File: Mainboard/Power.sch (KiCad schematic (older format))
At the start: 21 parts, among them Q1 P-Channel, U11 LP5907MFX-3.3, U4 TPS62175DQC, U5 TPS2113A

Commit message: Modify library references
As described in the README of the newly added libraries submodule.
Schematic and PCB are synced.

Hardware folder is renamed to mainboard
Any other PCBs can be put in their own subfolder in the gitrepo

Commit also swaps source/drain of Q1 because it appeared wrong for some
reason after updating all symbol/footprints.
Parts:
- L1: footprint ZOUDIOfootprints:SRN4012TA -> ZOUDIO-footprints:SRN4012TA
- Q1: footprint ZOUDIOfootprints:SOIC8_mosfet -> ZOUDIO-footprints:SOIC8_mosfet; symbol ZOUDIOsymbols:P-channel_SOIC -> Device:Q_PMOS_GSD
- U5: symbol ZOUDIOsymbols:TPS2113A -> ZOUDIO-symbols:TPS2113A
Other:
- moved on the sheet: R1
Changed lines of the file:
@@
 $EndDescr
-$Comp
-L ZOUDIOsymbols:P-channel_SOIC Q?
-U 1 1 60B84DA8
-P 2650 5000
-AR Path="/60B84DA8" Ref="Q?"  Part="1"
-AR Path="/60AAD6DF/60B84DA8" Ref="Q?"  Part="1"
-AR Path="/60B7AC16/60B84DA8" Ref="Q1"  Part="1"
-F 0 "Q1" H 2650 5247 60  0000 C CNN
-F 1 "P-Channel" H 2650 5141 60  0000 C CNN
-F 2 "ZOUDIOfootprints:SOIC8_mosfet" H 2650 5000 60  0001 C CNN
-F 3 "" H 2650 5000 60  0001 C CNN
-	1    2650 5000
-	-1   0    0    -1
-$EndComp
 $Comp
 L Device:R_Small R?
 U 1 1 60B84DAE
-P 2650 5450
+P 2650 5500
 AR Path="/60B84DAE" Ref="R?"  Part="1"
 AR Path="/60AAD6DF/60B84DAE" Ref="R?"  Part="1"
 AR Path="/60B7AC16/60B84DAE" Ref="R1"  Part="1"
-F 0 "R1" H 2709 5496 50  0000 L CNN
-F 1 "1M" H 2709 5405 50  0000 L CNN
-F 2 "Resistor_SMD:R_0603_1608Metric" H 2650 5450 50  0001 C CNN
-F 3 "~" H 2650 5450 50  0001 C CNN
-	1    2650 5450
+F 0 "R1" H 2709 5546 50  0000 L CNN
+F 1 "1M" H 2709 5455 50  0000 L CNN
+F 2 "Resistor_SMD:R_0603_1608Metric" H 2650 5500 50  0001 C CNN
+F 3 "~" H 2650 5500 50  0001 C CNN
+	1    2650 5500
 	1    0    0    -1
 $EndComp
@@
 L power:GND #PWR?
 U 1 1 60B84DB4
-P 2650 5600
+P 2650 5650
 AR Path="/60B84DB4" Ref="#PWR?"  Part="1"
 AR Path="/60AAD6DF/60B84DB4" Ref="#PWR?"  Part="1"
 AR Path="/60B7AC16/60B84DB4" Ref="#PWR0124"  Part="1"
-F 0 "#PWR0124" H 2650 5350 50  0001 C CNN
-F 1 "GND" H 2655 5427 50  0001 C CNN
-F 2 "" H 2650 5600 50  0001 C CNN
-F 3 "" H 2650 5600 50  0001 C CNN
-	1    2650 5600
-	1    0    0    -1
-$EndComp
-Wire Wire Line
-	2650 5600 2650 5550
+F 0 "#PWR0124" H 2650 5400 50  0001 C CNN
+F 1 "GND" H 2655 5477 50  0001 C CNN
+F 2 "" H 2650 5650 50  0001 C CNN
+F 3 "" H 2650 5650 50  0001 C CNN
+	1    2650 5650
+	1    0    0    -1
+$EndComp
+Wire Wire Line
+	2650 5650 2650 5600
 $Comp
 L power:GND #PWR?
 U 1 1 60B84DBC
-P 2350 5600
+P 2350 5650
 AR Path="/60B84DBC" Ref="#PWR?"  Part="1"
 AR Path="/60AAD6DF/60B84DBC" Ref="#PWR?"  Part="1"
 AR Path="/60B7AC16/60B84DBC" Ref="#PWR0125"  Part="1"
-F 0 "#PWR0125" H 2350 5350 50  0001 C CNN
-F 1 "GND" H 2355 5427 50  0001 C CNN
-F 2 "" H 2350 5600 50  0001 C CNN
-F 3 "" H 2350 5600 50  0001 C CNN
-	1    2350 5600
+F 0 "#PWR0125" H 2350 5400 50  0001 C CNN
+F 1 "GND" H 2355 5477 50  0001 C CNN
+F 2 "" H 2350 5650 50  0001 C CNN
+F 3 "" H 2350 5650 50  0001 C CNN
+	1    2350 5650
 	1    0    0    -1
 $EndComp
@@
 	2350 5000 2350 5150
 Wire Wire Line
-	2350 5450 2350 5600
-Wire Wire Line
 	2900 5050 2900 5000
 Wire Wire Line
 	2900 5000 2850 5000
 Wire Wire Line
-	2900 5250 2900 5300
-Wire Wire Line
-	2900 5300 2650 5300
-Wire Wire Line
 	2650 5300 2650 5350
-Wire Wire Line
-	2650 5300 2650 5250
-Connection ~ 2650 5300
 $Comp
 L Device:R_Small R?
@@
 	2000 4650 3400 4650
 Wire Notes Line
-	3400 4650 3400 5750
-Wire Notes Line
-	3400 5750 2000 5750
-Wire Notes Line
-	2000 5750 2000 4650
+	3400 4650 3400 5800
+Wire Notes Line
+	3400 5800 2000 5800
+Wire Notes Line
+	2000 5800 2000 4650
 Wire Wire Line
 	3000 5000 2900 5000
@@
 	7800 3600 7750 3600
 $Comp
-L ZOUDIOsymbols:TPS2113A U5
+L ZOUDIO-symbols:TPS2113A U5
 U 1 1 60AE2F0A
 P 7150 3700
@@
 F 0 "L1" V 4450 3350 50  0000 C CNN
 F 1 "10u" V 4350 3350 50  0000 C CNN
-F 2 "ZOUDIOfootprints:SRN4012TA" H 4250 3350 50  0001 C CNN
+F 2 "ZOUDIO-footprints:SRN4012TA" H 4250 3350 50  0001 C CNN
 F 3 "~" H 4250 3350 50  0001 C CNN
 	1    4250 3350
@@
 Wire Notes Line
 	5650 4650 4650 4650
+$Comp
+L Device:Q_PMOS_GSD Q?
+U 1 1 60B84DA8
+P 2650 5100
+AR Path="/60B84DA8" Ref="Q?"  Part="1"
+AR Path="/60AAD6DF/60B84DA8" Ref="Q?"  Part="1"
+AR Path="/60B7AC16/60B84DA8" Ref="Q1"  Part="1"
+F 0 "Q1" V 3000 5100 60  0000 C CNN
+F 1 "P-Channel" V 2900 5100 60  0000 C CNN
+F 2 "ZOUDIO-footprints:SOIC8_mosfet" H 2650 5100 60  0001 C CNN
+F 3 "" H 2650 5100 60  0001 C CNN
+	1    2650 5100
+	0    -1   -1   0
+$EndComp
+Wire Wire Line
+	2650 5350 2900 5350
+Wire Wire Line
+	2900 5250 2900 5350
+Wire Wire Line
+	2350 5450 2350 5650
+Wire Wire Line
+	2650 5350 2650 5400
+Connection ~ 2650 5350
 $EndSCHEMATC

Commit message: Before power tree change
Backup before switching from two to one LDO
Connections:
- net 5V_usb renamed VBUS
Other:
- note removed: "ERC"
- moved on the sheet: R5, R6
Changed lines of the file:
@@
 Sheet 4 9
 Title "4x38W amp with DSP and BT"
-Date "2021-06-08"
-Rev "0.1"
+Date "2021-11-08"
+Rev "0.2"
 Comp "ZOUDIO"
 Comment1 ""
@@
 L power:VDD #PWR0130
 U 1 1 60BA4A1D
-P 3800 4900
-F 0 "#PWR0130" H 3800 4750 50  0001 C CNN
-F 1 "VDD" H 3817 5073 50  0000 C CNN
-F 2 "" H 3800 4900 50  0001 C CNN
-F 3 "" H 3800 4900 50  0001 C CNN
-	1    3800 4900
+P 4000 4900
+F 0 "#PWR0130" H 4000 4750 50  0001 C CNN
+F 1 "VDD" H 4017 5073 50  0000 C CNN
+F 2 "" H 4000 4900 50  0001 C CNN
+F 3 "" H 4000 4900 50  0001 C CNN
+	1    4000 4900
 	1    0    0    -1
 $EndComp
@@
 L power:GND #PWR0131
 U 1 1 60BA4A23
-P 3800 5500
-F 0 "#PWR0131" H 3800 5250 50  0001 C CNN
-F 1 "GND" V 3805 5372 50  0001 R CNN
-F 2 "" H 3800 5500 50  0001 C CNN
-F 3 "" H 3800 5500 50  0001 C CNN
-	1    3800 5500
+P 4000 5500
+F 0 "#PWR0131" H 4000 5250 50  0001 C CNN
+F 1 "GND" V 4005 5372 50  0001 R CNN
+F 2 "" H 4000 5500 50  0001 C CNN
+F 3 "" H 4000 5500 50  0001 C CNN
+	1    4000 5500
 	1    0    0    -1
 $EndComp
@@
 L Device:R_Small R5
 U 1 1 60BA4A29
-P 3800 5050
-F 0 "R5" H 3859 5096 50  0000 L CNN
-F 1 "1M" H 3859 5005 50  0000 L CNN
-F 2 "Resistor_SMD:R_0603_1608Metric" H 3800 5050 50  0001 C CNN
-F 3 "~" H 3800 5050 50  0001 C CNN
-	1    3800 5050
+P 4000 5050
+F 0 "R5" H 4059 5096 50  0000 L CNN
+F 1 "1M" H 4059 5005 50  0000 L CNN
+F 2 "Resistor_SMD:R_0603_1608Metric" H 4000 5050 50  0001 C CNN
+F 3 "~" H 4000 5050 50  0001 C CNN
+	1    4000 5050
 	1    0    0    -1
 $EndComp
@@
 L Device:R_Small R6
 U 1 1 60BA4A2F
-P 3800 5350
-F 0 "R6" H 3859 5396 50  0000 L CNN
-F 1 "100k" H 3859 5305 50  0000 L CNN
-F 2 "Resistor_SMD:R_0603_1608Metric" H 3800 5350 50  0001 C CNN
-F 3 "~" H 3800 5350 50  0001 C CNN
-	1    3800 5350
-	1    0    0    -1
-$EndComp
-Wire Wire Line
-	3800 4900 3800 4950
-Wire Wire Line
-	3800 5150 3800 5200
-Wire Wire Line
-	3850 5200 3800 5200
-Connection ~ 3800 5200
-Wire Wire Line
-	3800 5200 3800 5250
-Wire Wire Line
-	3800 5450 3800 5500
-Wire Notes Line
-	3650 5650 3650 4650
-Text HLabel 3850 5200 2    50   Output ~ 0
+P 4000 5350
+F 0 "R6" H 4059 5396 50  0000 L CNN
+F 1 "100k" H 4059 5305 50  0000 L CNN
+F 2 "Resistor_SMD:R_0603_1608Metric" H 4000 5350 50  0001 C CNN
+F 3 "~" H 4000 5350 50  0001 C CNN
+	1    4000 5350
+	1    0    0    -1
+$EndComp
+Wire Wire Line
+	4000 4900 4000 4950
+Wire Wire Line
+	4000 5150 4000 5200
+Wire Wire Line
+	4050 5200 4000 5200
+Connection ~ 4000 5200
+Wire Wire Line
+	4000 5200 4000 5250
+Wire Wire Line
+	4000 5450 4000 5500
+Wire Notes Line
+	3850 5650 3850 4650
+Text HLabel 4050 5200 2    50   Output ~ 0
 VDD_divider
 Text GLabel 2300 5000 0    50   Input ~ 0
 Vin
 Wire Notes Line
-	4400 4650 4400 5650
-Wire Notes Line
-	3650 4650 4400 4650
-Wire Notes Line
-	3650 5650 4400 5650
-Text Notes 3650 4650 0    50   ~ 0
+	4600 4650 4600 5650
+Wire Notes Line
+	3850 4650 4600 4650
+Wire Notes Line
+	3850 5650 4600 5650
+Text Notes 3850 4650 0    50   ~ 0
 VDD divider
 Wire Notes Line
-	2000 4650 3400 4650
-Wire Notes Line
-	3400 4650 3400 5800
-Wire Notes Line
-	3400 5800 2000 5800
+	2000 4650 3600 4650
+Wire Notes Line
+	3600 4650 3600 5800
+Wire Notes Line
+	3600 5800 2000 5800
 Wire Notes Line
 	2000 5800 2000 4650
@@
 Text Label 6200 3400 2    50   ~ 0
 5V_buck
-Text GLabel 7750 3400 2    50   Input ~ 0
-5V_usb
 Text Notes 5800 3000 0    50   ~ 0
 5V multiplexer
@@
 Text Notes 5850 4500 0    50   ~ 0
 If VSNS < 0.8V (5V_buck < 4.55V) IN2 is selected
-Text GLabel 5000 4750 0    50   Input ~ 0
-5V_usb
-$Comp
-L power:PWR_FLAG #FLG?
-U 1 1 611046AD
-P 5050 4750
-AR Path="/60AA037E/611046AD" Ref="#FLG?"  Part="1"
-AR Path="/60B7AC16/611046AD" Ref="#FLG0102"  Part="1"
-F 0 "#FLG0102" H 5050 4825 50  0001 C CNN
-F 1 "PWR_FLAG" V 5050 4900 50  0000 L CNN
-F 2 "" H 5050 4750 50  0001 C CNN
-F 3 "~" H 5050 4750 50  0001 C CNN
-	1    5050 4750
-	0    1    1    0
-$EndComp
-Text Notes 4650 4650 0    50   ~ 0
-ERC
-Wire Wire Line
-	5000 4750 5050 4750
-Text Label 5000 4900 2    50   ~ 0
-5V_buck
 $Comp
 L power:PWR_FLAG #FLG?
 U 1 1 6110A1E3
-P 5050 4900
+P 4800 3300
 AR Path="/60AA037E/6110A1E3" Ref="#FLG?"  Part="1"
 AR Path="/60B7AC16/6110A1E3" Ref="#FLG0103"  Part="1"
-F 0 "#FLG0103" H 5050 4975 50  0001 C CNN
-F 1 "PWR_FLAG" V 5050 5050 50  0000 L CNN
-F 2 "" H 5050 4900 50  0001 C CNN
-F 3 "~" H 5050 4900 50  0001 C CNN
-	1    5050 4900
-	0    1    1    0
-$EndComp
-Wire Wire Line
-	5050 4900 5000 4900
-$Comp
-L power:VDD #PWR0170
-U 1 1 6110C56B
-P 5000 5050
-F 0 "#PWR0170" H 5000 4900 50  0001 C CNN
-F 1 "VDD" V 5000 5250 50  0000 C CNN
-F 2 "" H 5000 5050 50  0001 C CNN
-F 3 "" H 5000 5050 50  0001 C CNN
-	1    5000 5050
-	0    -1   -1   0
-$EndComp
-$Comp
-L power:PWR_FLAG #FLG?
-U 1 1 6110D265
-P 5050 5050
-AR Path="/60AA037E/6110D265" Ref="#FLG?"  Part="1"
-AR Path="/60B7AC16/6110D265" Ref="#FLG0104"  Part="1"
-F 0 "#FLG0104" H 5050 5125 50  0001 C CNN
-F 1 "PWR_FLAG" V 5050 5200 50  0000 L CNN
-F 2 "" H 5050 5050 50  0001 C CNN
-F 3 "~" H 5050 5050 50  0001 C CNN
-	1    5050 5050
-	0    1    1    0
-$EndComp
-Wire Wire Line
-	5050 5050 5000 5050
-Wire Notes Line
-	4650 4650 4650 5150
-Wire Notes Line
-	4650 5150 5650 5150
-Wire Notes Line
-	5650 5150 5650 4650
-Wire Notes Line
-	5650 4650 4650 4650
+F 0 "#FLG0103" H 4800 3375 50  0001 C CNN
+F 1 "PWR_FLAG" H 4800 3450 50  0000 C CNN
+F 2 "" H 4800 3300 50  0001 C CNN
+F 3 "~" H 4800 3300 50  0001 C CNN
+	1    4800 3300
+	1    0    0    -1
+$EndComp
 $Comp
 L Device:Q_PMOS_GSD Q?
@@
 	2650 5350 2650 5400
 Connection ~ 2650 5350
+$Comp
+L power:VBUS #PWR?
+U 1 1 618A3BA9
+P 7800 3350
+AR Path="/618A3BA9" Ref="#PWR?"  Part="1"
+AR Path="/60B7AC16/618A3BA9" Ref="#PWR?"  Part="1"
+F 0 "#PWR?" H 7800 3200 50  0001 C CNN
+F 1 "VBUS" H 7800 3500 50  0000 C CNN
+F 2 "" H 7800 3350 50  0001 C CNN
+F 3 "" H 7800 3350 50  0001 C CNN
+	1    7800 3350
+	1    0    0    -1
+$EndComp
+Wire Wire Line
+	7800 3350 7800 3400
+Wire Wire Line
+	7800 3400 7750 3400
+Wire Wire Line
+	4800 3300 4800 3350
+$Comp
+L power:PWR_FLAG #FLG?
+U 1 1 618CB810
+P 3350 4950
+AR Path="/60AA037E/618CB810" Ref="#FLG?"  Part="1"
+AR Path="/60B7AC16/618CB810" Ref="#FLG?"  Part="1"
+F 0 "#FLG?" H 3350 5025 50  0001 C CNN
+F 1 "PWR_FLAG" H 3350 5100 50  0000 C CNN
+F 2 "" H 3350 4950 50  0001 C CNN
+F 3 "~" H 3350 4950 50  0001 C CNN
+	1    3350 4950
+	1    0    0    -1
+$EndComp
+Wire Wire Line
+	3000 5000 3350 5000
+Wire Wire Line
+	3350 5000 3350 4950
+Connection ~ 3000 5000
 $EndSCHEMATC

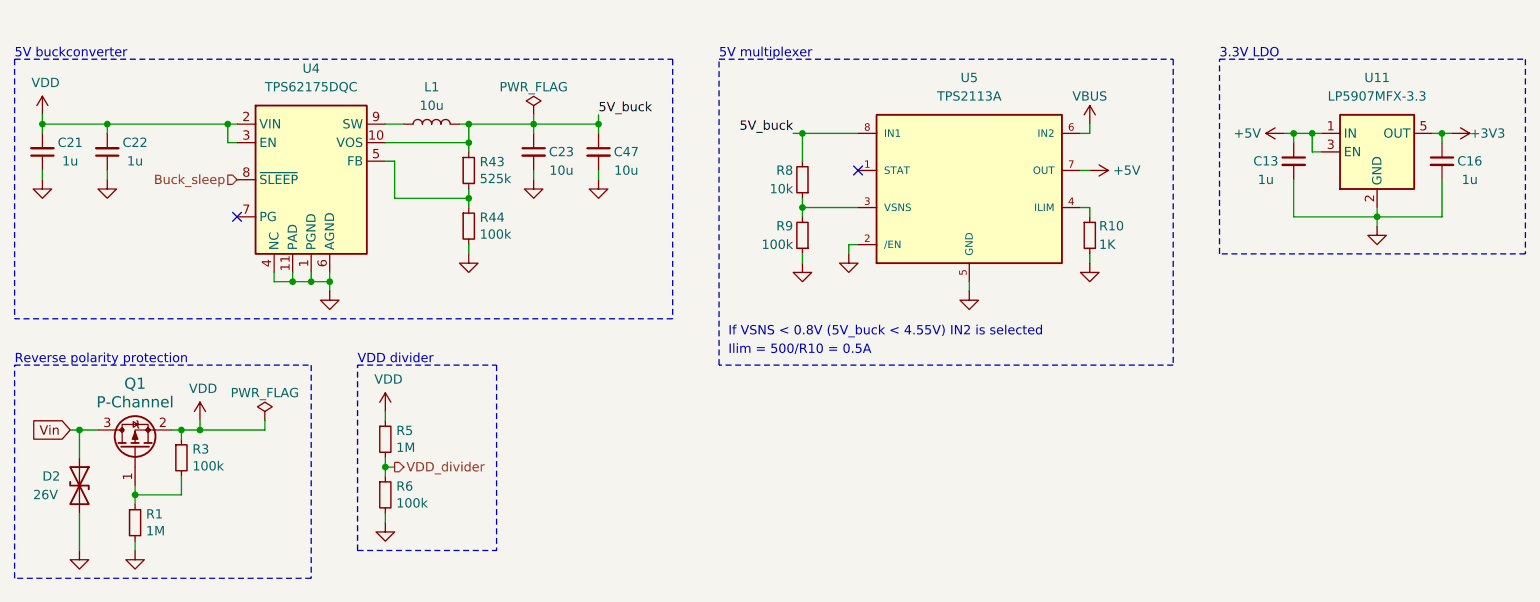
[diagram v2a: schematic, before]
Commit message: Before testing CH340B and VCHG
Cleaned up amp lay-out a bit in the meanwhile
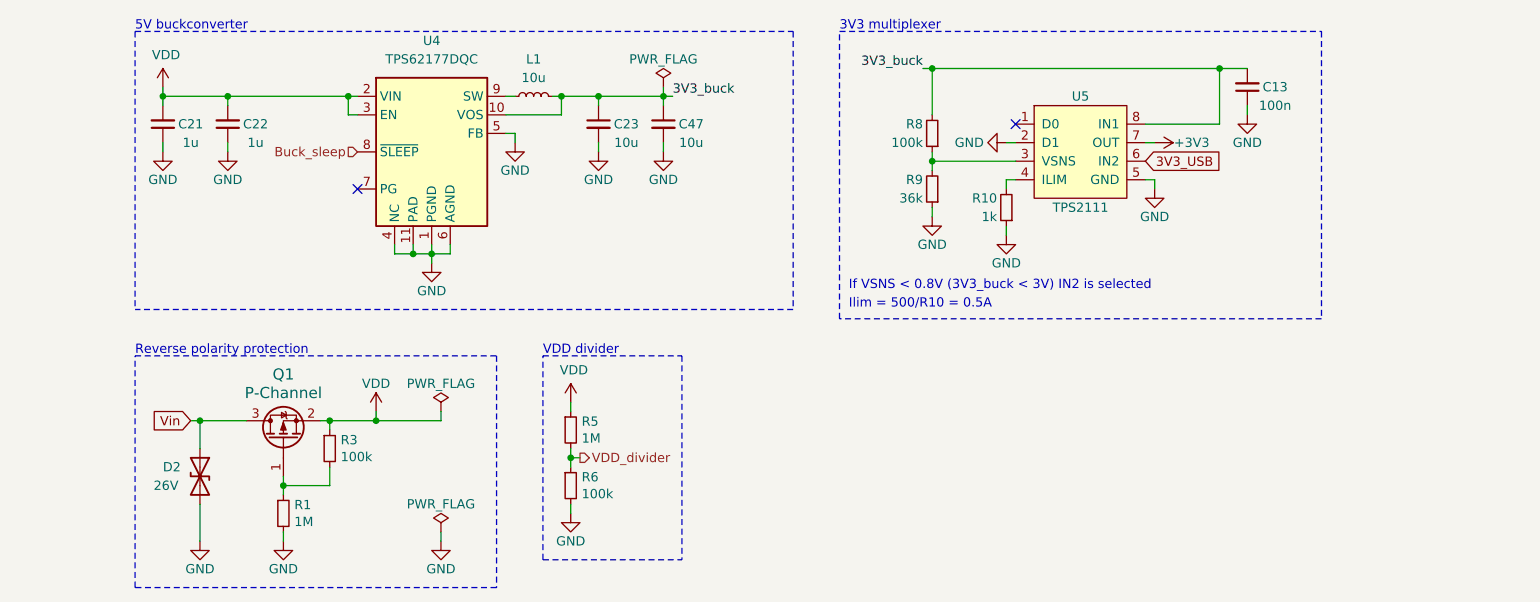
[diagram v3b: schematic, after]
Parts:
- removed C16: 1u, Capacitor_SMD:C_0805_2012Metric, symbol Device:C_Small
- removed L1: 10u, ZOUDIO-footprints:SRN4012TA, symbol Device:L
- removed R43: 525k, Resistor_SMD:R_0603_1608Metric, symbol Device:R_Small
- removed R44: 100k, Resistor_SMD:R_0603_1608Metric, symbol Device:R_Small
- removed U11: LP5907MFX-3.3, Package_TO_SOT_SMD:SOT-23-5, symbol Regulator_Linear:LP5907MFX-3.3
- removed U4: TPS62175DQC, Package_SON:WSON-10-1EP_2x3mm_P0.5mm_EP0.84x2.4mm_ThermalVias, symbol Regulator_Switching:TPS62175DQC
- removed U5: TPS2113A, Package_SO:TSSOP-8_3x3mm_P0.65mm, symbol ZOUDIO-symbols:TPS2113A
- added L1: 10u, Inductor_SMD:L_Bourns-SRN4018, symbol Device:L_Small
- added U4: TPS62177DQC, Package_SON:WSON-10-1EP_2x3mm_P0.5mm_EP0.84x2.4mm_ThermalVias, symbol Regulator_Switching:TPS62177DQC
- added U5: TPS2111, Package_SO:TSSOP-8_4.4x3mm_P0.65mm, symbol ZOUDIO-symbols:TPS211xA
- C13: value 1u -> 100n; footprint Capacitor_SMD:C_0805_2012Metric -> Capacitor_SMD:C_0603_1608Metric; Manufacturer (none) -> Murata; Partnumber (none) -> GCM188L81H104KA57D
- C21, C22: Manufacturer (none) -> Taiyo Yuden; Partnumber (none) -> UMK212B7105KG-T
- R10: value 1K -> 1k
- R8: value 10k -> 100k
- R9: value 100k -> 36k
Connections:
- net +5V is gone; now on net GND: C13.1
- net +3V3: now also U5.7 (OUT)
- net Buck_sleep: now also U4.8 (~SLEEP)
- net GND: now also R10.1, U4.1 (PGND), U4.11 (PAD), U4.4 (NC), U4.5 (FB), U4.6 (AGND), U5.2 (D1), U5.5 (GND); no longer C13.2, R10.2
- net VDD: now also U4.2 (VIN), U4.3 (EN)
- net at R8.1, R9.2: now also U5.3 (VSNS)
- net 5V_buck renamed 3V3_buck
- net 3V3_buck: now also C13.2, L1.2, U4.10 (VOS), U5.8 (IN1)
- new net: L1.1, U4.9 (SW)
- new net: R10.2, U5.4 (ILIM)
- new net 3V3_USB: U5.6 (IN2)
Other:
- note added: "3V3 multiplexer"
- note added: "If VSNS < 0.8V (3V3_buck < 3V) IN2 is selected"
- note removed: "3.3V LDO"
- note removed: "5V multiplexer"
- note removed: "If VSNS < 0.8V (5V_buck < 4.55V) IN2 is selected"
- moved on the sheet: C21, C22, C23, C47, D2, Q1, R1, R3, R5, R6, R8, R9

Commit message: Mainboard: Version 1.0
Still need to clean up 3D models and BoM list,
but gerberexport-ready and ready to order.
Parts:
- U4: footprint Package_SON:WSON-10-1EP_2x3mm_P0.5mm_EP0.84x2.4mm_ThermalVias -> ZOUDIO-footprints:WSON-10-1EP_2x3mm_P0.5mm_EP0.84x2.4mm
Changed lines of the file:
@@
 Sheet 3 11
 Title "4x38W amp with DSP and BT"
-Date "2021-11-19"
-Rev "0.2"
+Date "2021-12-01"
+Rev "1.0"
 Comp "ZOUDIO"
 Comment1 ""
@@
 F 0 "U4" H 4250 4100 50  0000 C CNN
 F 1 "TPS62177DQC" H 4250 4000 50  0000 C CNN
-F 2 "Package_SON:WSON-10-1EP_2x3mm_P0.5mm_EP0.84x2.4mm_ThermalVias" H 4400 3050 50  0001 L CNN
+F 2 "ZOUDIO-footprints:WSON-10-1EP_2x3mm_P0.5mm_EP0.84x2.4mm" H 4400 3050 50  0001 L CNN
 F 3 "http://www.ti.com/lit/ds/symlink/tps62177.pdf" H 4250 4050 50  0001 C CNN
 	1    4250 3500

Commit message: Clean up schematic for BoM export
- Change 22u 0805's (amp decoupling) to 15u
- Change 680n 0805's (part of output filter) to 470n
- Change C1 (amp bulk cap) from 820u to 1000u
- Add BoM.ini for KiBom export and
- Complete fields needed for KiBom (Manufacturer and partnumber)
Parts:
- C23, C47: Manufacturer (none) -> Samsung; Partnumber (none) -> CL21A106KPFNNNG
- D2: Manufacturer (none) -> Bourns; Partnumber (none) -> SMAJ26CA
- L1: Manufacturer (none) -> Bourns; Partnumber (none) -> SRN4012TA-100M
- Q1: Manufacturer (none) -> Infineon; Partnumber (none) -> IRF9393TRPBF
- R1, R5: Manufacturer (none) -> Yageo; Partnumber (none) -> RC0603FR-071ML
- R10: Manufacturer (none) -> Yageo; Partnumber (none) -> RC0603FR-071KL
- R3, R6, R8: Manufacturer (none) -> Yageo; Partnumber (none) -> RC0603FR-07100KL
- R9: Manufacturer (none) -> Yageo; Partnumber (none) -> RC0603FR-0736KL
- U4: value TPS62177DQC -> TPS62177; Manufacturer (none) -> Texas Instruments; Partnumber (none) -> TPS62177DQCR
- U5: Manufacturer (none) -> Texas Instruments; Partnumber (none) -> TPS2111APWR
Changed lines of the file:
@@
 F 2 "Resistor_SMD:R_0603_1608Metric" H 3450 5450 50  0001 C CNN
 F 3 "~" H 3450 5450 50  0001 C CNN
+F 4 "Yageo" H 3450 5450 50  0001 C CNN "Manufacturer"
+F 5 "RC0603FR-071ML" H 3450 5450 50  0001 C CNN "Partnumber"
 	1    3450 5450
 	1    0    0    -1
@@
 F 2 "Diode_SMD:D_SMA" H 3000 5250 50  0001 C CNN
 F 3 "~" H 3000 5250 50  0001 C CNN
+F 4 "Bourns" H 3000 5250 50  0001 C CNN "Manufacturer"
+F 5 "SMAJ26CA" H 3000 5250 50  0001 C CNN "Partnumber"
 	1    3000 5250
 	0    1    1    0
@@
 F 2 "Resistor_SMD:R_0603_1608Metric" H 3700 5100 50  0001 C CNN
 F 3 "~" H 3700 5100 50  0001 C CNN
+F 4 "Yageo" H 3700 5100 50  0001 C CNN "Manufacturer"
+F 5 "RC0603FR-07100KL" H 3700 5100 50  0001 C CNN "Partnumber"
 	1    3700 5100
 	1    0    0    -1
@@
 F 2 "Resistor_SMD:R_0603_1608Metric" H 5000 5000 50  0001 C CNN
 F 3 "~" H 5000 5000 50  0001 C CNN
+F 4 "Yageo" H 5000 5000 50  0001 C CNN "Manufacturer"
+F 5 "RC0603FR-071ML" H 5000 5000 50  0001 C CNN "Partnumber"
 	1    5000 5000
 	1    0    0    -1
@@
 F 2 "Resistor_SMD:R_0603_1608Metric" H 5000 5300 50  0001 C CNN
 F 3 "~" H 5000 5300 50  0001 C CNN
+F 4 "Yageo" H 5000 5300 50  0001 C CNN "Manufacturer"
+F 5 "RC0603FR-07100KL" H 5000 5300 50  0001 C CNN "Partnumber"
 	1    5000 5300
 	1    0    0    -1
@@
 F 2 "Resistor_SMD:R_0603_1608Metric" H 6950 3700 50  0001 C CNN
 F 3 "~" H 6950 3700 50  0001 C CNN
+F 4 "Yageo" H 6950 3700 50  0001 C CNN "Manufacturer"
+F 5 "RC0603FR-0736KL" H 6950 3700 50  0001 C CNN "Partnumber"
 	1    6950 3700
 	-1   0    0    1
@@
 F 2 "Resistor_SMD:R_0603_1608Metric" H 6950 3400 50  0001 C CNN
 F 3 "~" H 6950 3400 50  0001 C CNN
+F 4 "Yageo" H 6950 3400 50  0001 C CNN "Manufacturer"
+F 5 "RC0603FR-07100KL" H 6950 3400 50  0001 C CNN "Partnumber"
 	1    6950 3400
 	-1   0    0    1
@@
 F 2 "Capacitor_SMD:C_0805_2012Metric" H 5500 3350 50  0001 C CNN
 F 3 "~" H 5500 3350 50  0001 C CNN
+F 4 "Samsung" H 5500 3350 50  0001 C CNN "Manufacturer"
+F 5 "CL21A106KPFNNNG" H 5500 3350 50  0001 C CNN "Partnumber"
 	1    5500 3350
 	1    0    0    -1
@@
 F 2 "Capacitor_SMD:C_0805_2012Metric" H 5150 3350 50  0001 C CNN
 F 3 "~" H 5150 3350 50  0001 C CNN
+F 4 "Samsung" H 5150 3350 50  0001 C CNN "Manufacturer"
+F 5 "CL21A106KPFNNNG" H 5150 3350 50  0001 C CNN "Partnumber"
 	1    5150 3350
 	1    0    0    -1
@@
 F 2 "ZOUDIO-footprints:SOIC8_mosfet" H 3450 5050 60  0001 C CNN
 F 3 "" H 3450 5050 60  0001 C CNN
+F 4 "Infineon" H 3450 5050 50  0001 C CNN "Manufacturer"
+F 5 "IRF9393TRPBF" H 3450 5050 50  0001 C CNN "Partnumber"
 	1    3450 5050
 	0    -1   -1   0
@@
 F 2 "Inductor_SMD:L_Bourns-SRN4018" H 4800 3200 50  0001 C CNN
 F 3 "~" H 4800 3200 50  0001 C CNN
+F 4 "Bourns" H 4800 3200 50  0001 C CNN "Manufacturer"
+F 5 "SRN4012TA-100M" H 4800 3200 50  0001 C CNN "Partnumber"
 	1    4800 3200
 	0    -1   -1   0
@@
 F 2 "Package_SO:TSSOP-8_4.4x3mm_P0.65mm" H 7750 3500 50  0001 C CNN
 F 3 "" H 7750 3500 50  0001 C CNN
+F 4 "Texas Instruments" H 7750 3500 50  0001 C CNN "Manufacturer"
+F 5 "TPS2111APWR" H 7750 3500 50  0001 C CNN "Partnumber"
 	1    7750 3500
 	1    0    0    -1
@@
 F 2 "Resistor_SMD:R_0603_1608Metric" H 7350 3800 50  0001 C CNN
 F 3 "~" H 7350 3800 50  0001 C CNN
+F 4 "Yageo" H 7350 3800 50  0001 C CNN "Manufacturer"
+F 5 "RC0603FR-071KL" H 7350 3800 50  0001 C CNN "Partnumber"
 	1    7350 3800
 	-1   0    0    1
@@
 P 4250 3500
 F 0 "U4" H 4250 4100 50  0000 C CNN
-F 1 "TPS62177DQC" H 4250 4000 50  0000 C CNN
+F 1 "TPS62177" H 4250 4000 50  0000 C CNN
 F 2 "ZOUDIO-footprints:WSON-10-1EP_2x3mm_P0.5mm_EP0.84x2.4mm" H 4400 3050 50  0001 L CNN
 F 3 "http://www.ti.com/lit/ds/symlink/tps62177.pdf" H 4250 4050 50  0001 C CNN
+F 4 "Texas Instruments" H 4250 3500 50  0001 C CNN "Manufacturer"
+F 5 "TPS62177DQCR" H 4250 3500 50  0001 C CNN "Partnumber"
 	1    4250 3500
 	1    0    0    -1
